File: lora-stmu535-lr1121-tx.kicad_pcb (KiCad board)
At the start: 4 copper layers, 111 parts, among them J1 Conn_Coaxial_Small, J2 Conn_02x07_Odd_Even, J4 USB_C_Receptacle_USB2.0_16P, J5 2.4Ghz Antenna, J6 Conn_01x03_Pin, J7 Conn_02x06_Counter_Clockwise, SW3 SW_Push, U1 BME280, U2 BGS12WN6E6327, U3 BQ25570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

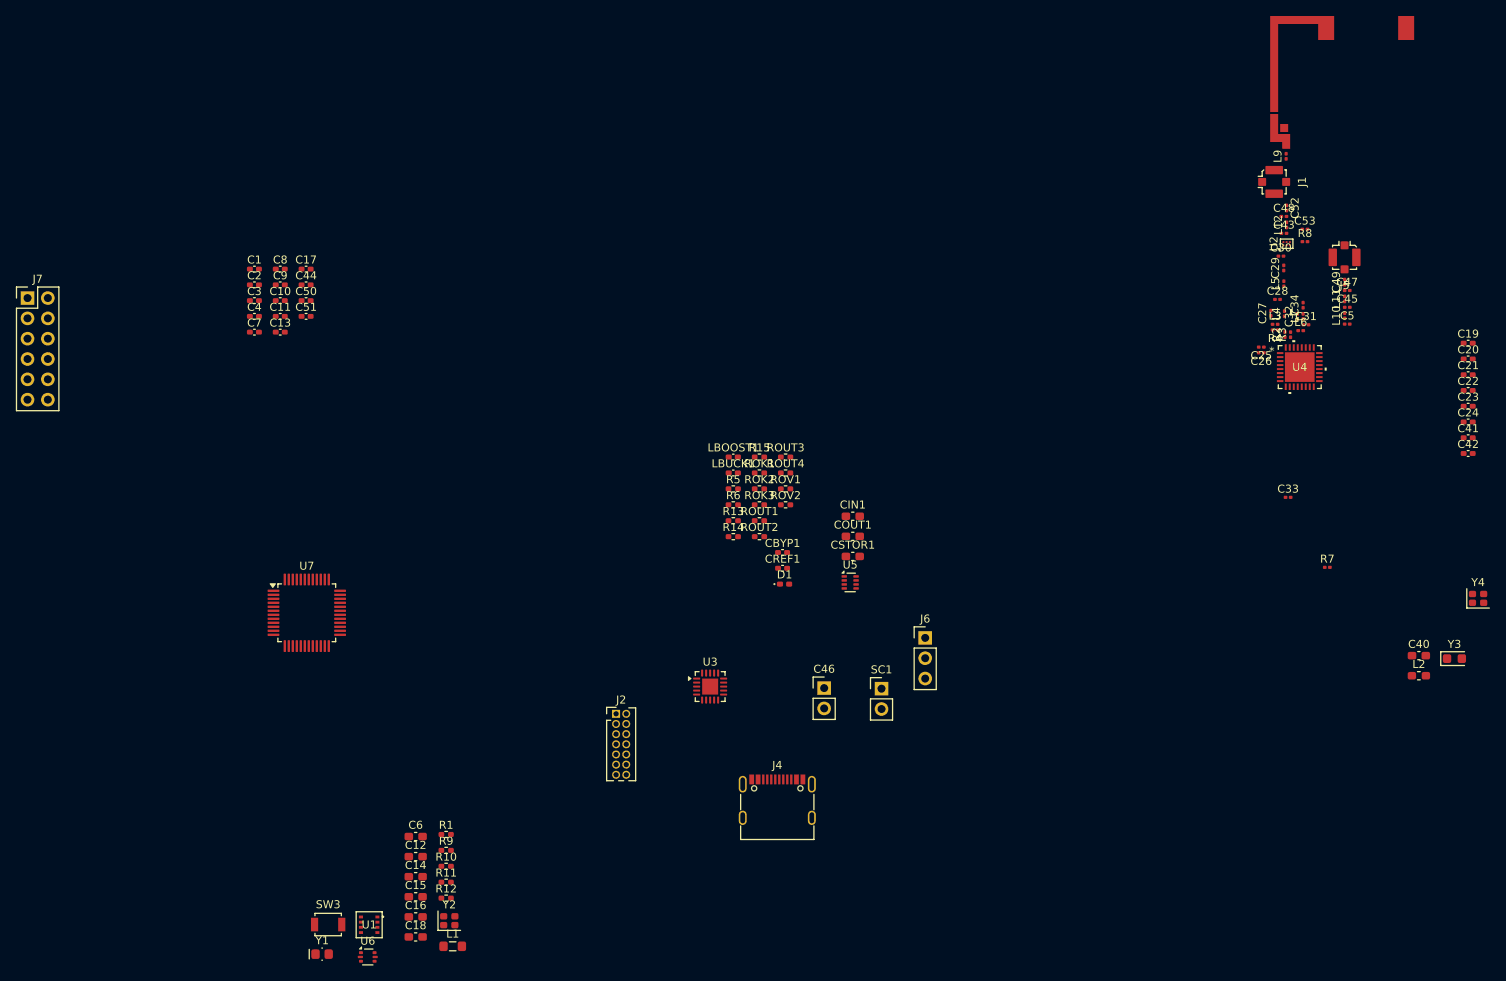
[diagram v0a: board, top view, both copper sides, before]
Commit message: RF and initial routing
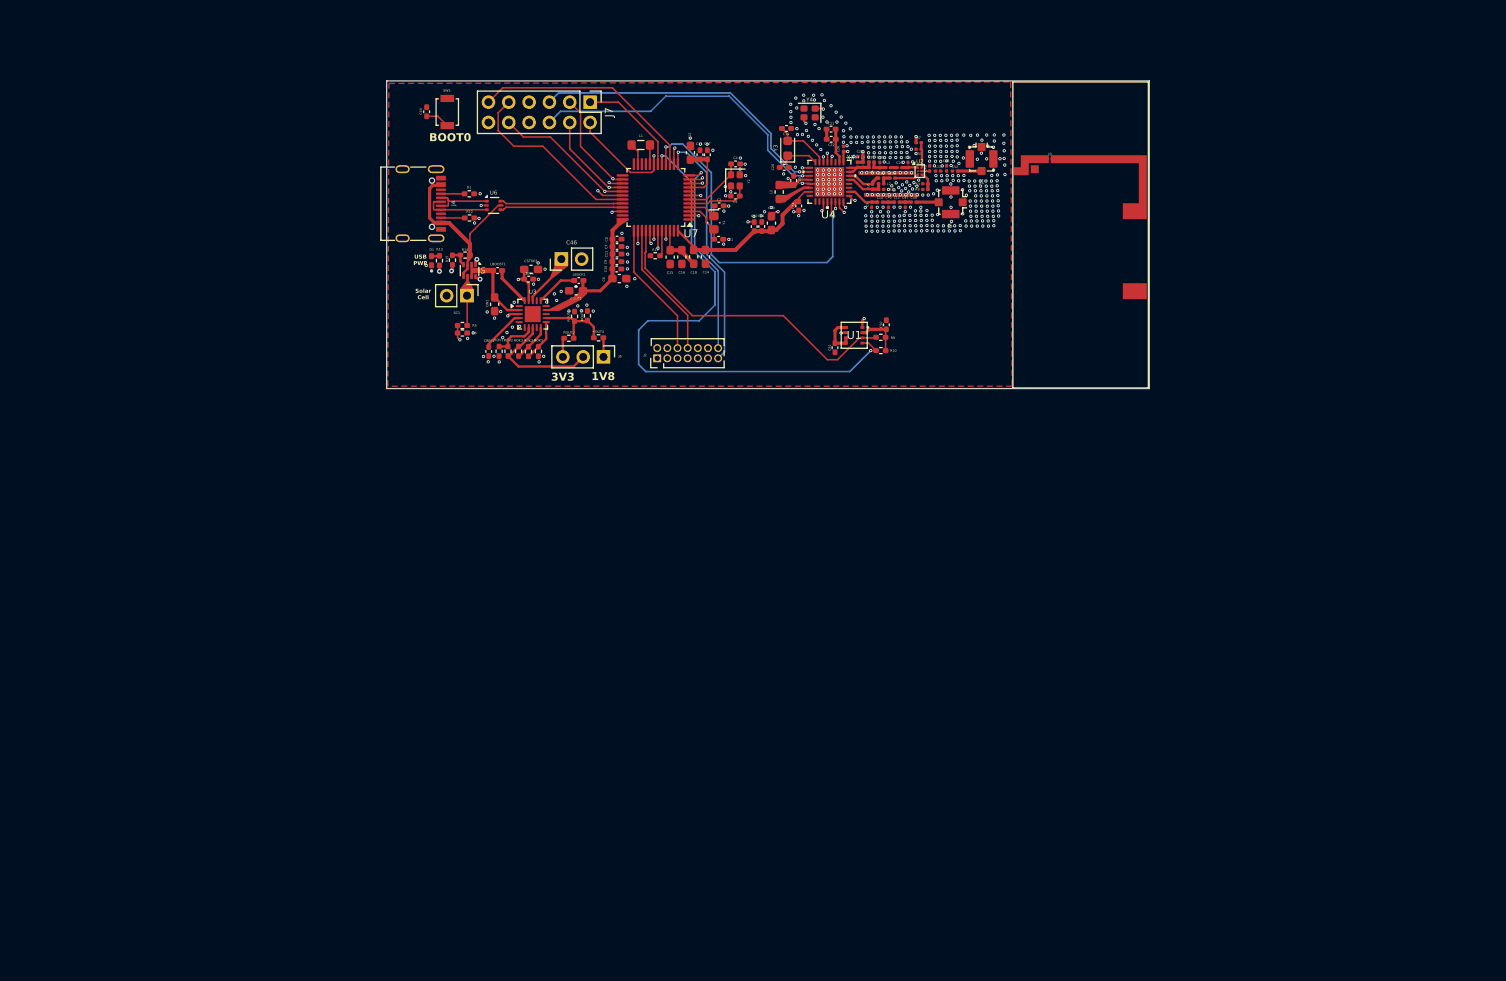
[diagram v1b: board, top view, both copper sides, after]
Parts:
- removed R2, R3: 0R, Resistor_SMD:R_0201_0603Metric
- moved Y3 105.0 mm to (149.4, 59.7), turned to 90 degrees
- moved Y1 103.7 mm to (140.1, 69.0), turned to -90 degrees
- moved Y4 103.3 mm to (152.1, 55.3), turned to 180 degrees
- moved L1 102.9 mm to (131.0, 59.3), turned to 180 degrees
- moved SW3 102.6 mm to (106.8, 55.2), turned to 90 degrees
- moved L2 100.2 mm to (148.3, 65.2), turned to 90 degrees
- moved Y2 99.2 mm to (142.8, 63.7), turned to -90 degrees
- moved C40 97.3 mm to (147.3, 69.1), turned to 90 degrees
- moved U1 95.4 mm to (157.7, 83.1)
- moved U6 95.3 mm to (112.6, 66.9)
- moved C12 94.4 mm to (137.2, 60.3), turned to 90 degrees
- moved C42 93.6 mm to (145.2, 69.5), turned to 90 degrees
- moved C41 92.2 mm to (146.1, 69.5), turned to 90 degrees
- moved C18 91.8 mm to (137.6, 73.3), turned to -90 degrees
- moved C19 89.3 mm to (149.2, 57.2), turned to 180 degrees
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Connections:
- C27 pad 1: Net-(C27-Pad1) -> Net-(U4-RFO_HP_LF)
- J4 pad A6: /MCU/D+ -> Net-(J4-D+-PadA6)
- J4 pad A7: /MCU/D- -> Net-(J4-D--PadA7)
- J4 pad B6: /MCU/D+ -> Net-(J4-D+-PadA6)
- J4 pad B7: /MCU/D- -> Net-(J4-D--PadA7)
- L3 pad 2: Net-(C27-Pad1) -> Net-(U4-RFO_HP_LF)
- L4 pad 1: Net-(C27-Pad1) -> Net-(U4-RFO_HP_LF)
- R4 pad 1: Net-(C27-Pad1) -> Net-(U4-RFO_HP_LF)
- U4 pad 31: Net-(U4-RFO_LP_LF) -> Net-(U4-RFO_HP_LF)
- U6 pad 1: Net-(U7-PA11) -> Net-(J4-D--PadA7)
- U6 pad 3: Net-(U7-PA12) -> Net-(J4-D+-PadA6)
- U6 pad 5: unconnected-(U6-VBUS-Pad5) -> 5V
- U7 pad 32: Net-(U7-PA11) -> /MCU/D-
- U7 pad 33: Net-(U7-PA12) -> /MCU/D+
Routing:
- net SCL: track 0.00 -> 71.0 mm, vias 0 -> 2
- net VBAT: track 0.00 -> 55.1 mm
- net LR_MISO: track 0.00 -> 42.6 mm, vias 0 -> 2
- net SDA: track 0.00 -> 39.5 mm
- net DIO7: track 0.00 -> 39.2 mm, vias 0 -> 1
- net DIO8: track 0.00 -> 38.2 mm, vias 0 -> 1
- net LR_BUSY: track 0.00 -> 36.7 mm, vias 0 -> 2
- net LR_CS: track 0.00 -> 35.1 mm, vias 0 -> 2
- net LR_MOSI: track 0.00 -> 34.5 mm, vias 0 -> 2
- net LR_NRESET: track 0.00 -> 34.0 mm, vias 0 -> 2
- net /MCU/PA0: track 0.00 -> 32.8 mm, vias 0 -> 1
- net /MCU/LPUART_RX: track 0.00 -> 30.6 mm, vias 0 -> 1
- net DIO9: track 0.00 -> 29.0 mm, vias 0 -> 2
- net /MCU/PA5: track 0.00 -> 28.8 mm
- net /MCU/LPUART_TX: track 0.00 -> 25.1 mm, vias 0 -> 1
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- added copper zone on F.Cu, net GND
- added copper zone on In1.Cu, net GND
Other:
- board outline added: 95.3 x 38.4 mm
- board text added: "1V8"
- board text added: "3V3"
- board text added: "BOOT0"
- board text added: "CHECK CLOCK, CHOOSE TCXO/XTAL"
- board text added: "Posso far passare sotto senza problemi?"
- board text added: "Solar Cell"
- board text added: "TODO: - Finish RF - GND - Signal routing - Labeling"
- board text added: "USB PWR"

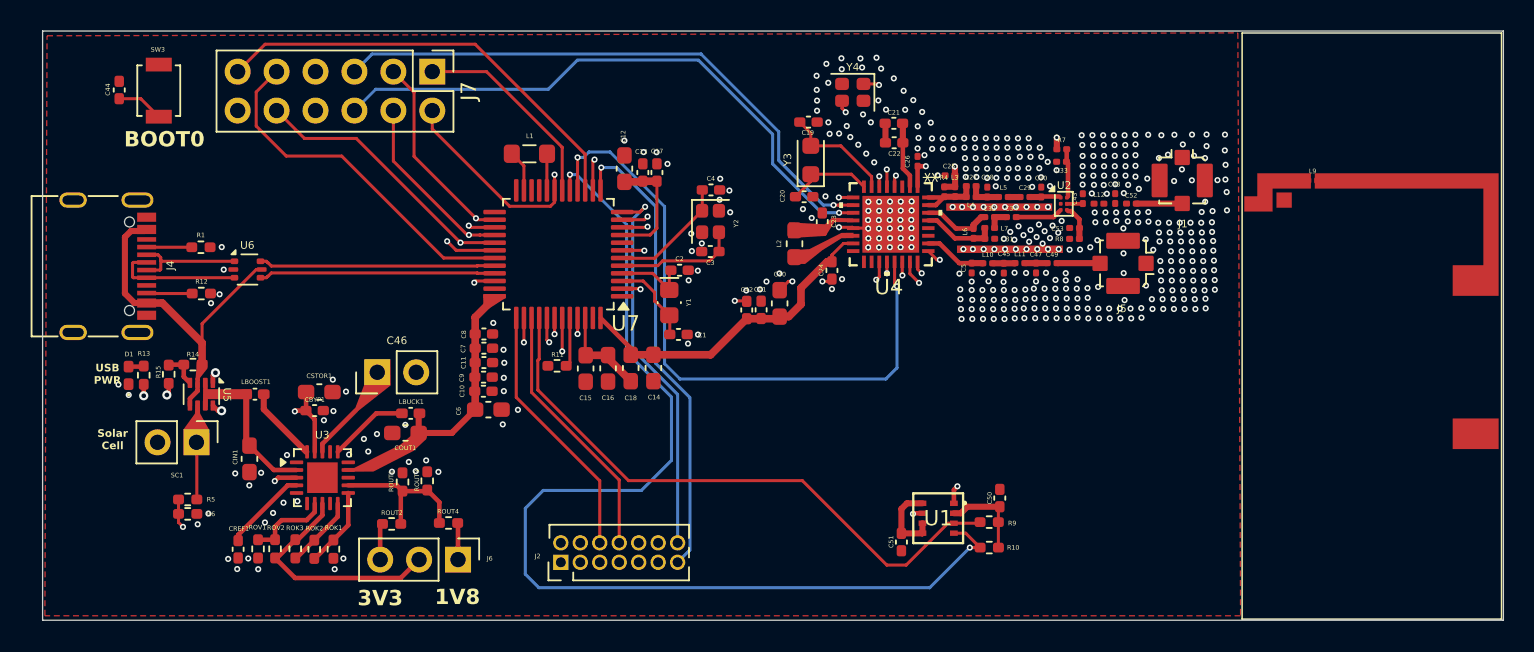
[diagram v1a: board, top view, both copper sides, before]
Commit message: fix DRC errors and antenna
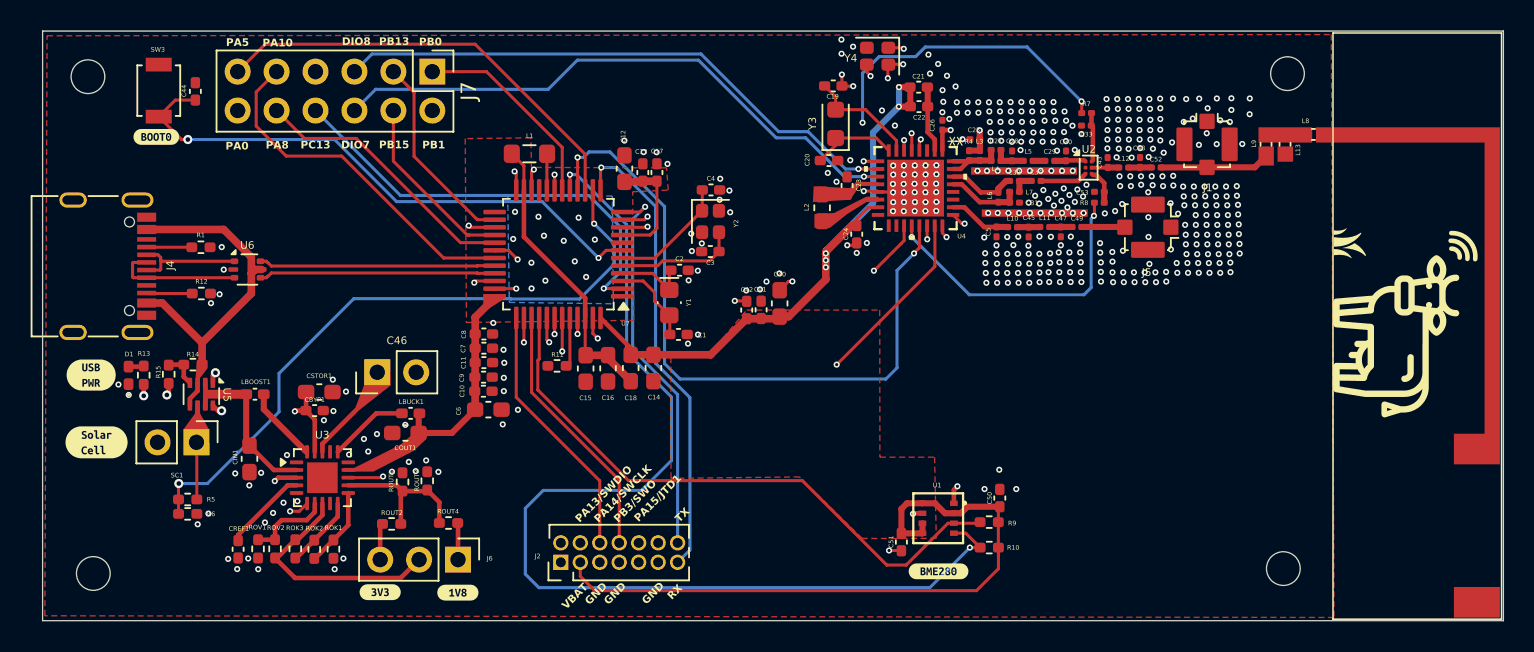
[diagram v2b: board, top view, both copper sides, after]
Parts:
- added L13: 7nH, Inductor_SMD:L_0402_1005Metric_Pad0.77x0.64mm_HandSolder, F.Cu at (180.3, 58.7)
- added L8: 13nH, Inductor_SMD:L_0402_1005Metric_Pad0.77x0.64mm_HandSolder, F.Cu at (182.2, 58.0)
- added REF**: MountingHole_2.2mm_M2, MountingHole:MountingHole_2.2mm_M2, F.Cu at (102.2, 54.3)
- added REF**: MountingHole_2.2mm_M2, MountingHole:MountingHole_2.2mm_M2, F.Cu at (180.5, 54.1)
- added REF**: cow_logo, cowtag:cow_logo, F.Cu at (187.8, 72.3)
- added REF**: MountingHole_2.2mm_M2, MountingHole:MountingHole_2.2mm_M2, F.Cu at (102.6, 86.7)
- added REF**: MountingHole_2.2mm_M2, MountingHole:MountingHole_2.2mm_M2, F.Cu at (180.2, 86.4)
- added REF**: leat, cowtag:leat, B.Cu at (165.7, 85.9)
- added kibuzzard-69E8EEB9: G***, kibuzzard-69E8EEB9, F.Cu at (157.7, 86.5)
- added kibuzzard-69E8EEEB: G***, kibuzzard-69E8EEEB, F.Cu at (121.3, 87.9)
- added kibuzzard-69E8EEF7: G***, kibuzzard-69E8EEF7, F.Cu at (126.3, 87.9)
- added kibuzzard-69E8EF24: G***, kibuzzard-69E8EF24, F.Cu at (102.4, 73.7)
- added kibuzzard-69E8EF49: G***, kibuzzard-69E8EF49, F.Cu at (102.8, 78.1)
- added kibuzzard-69E8EF58: G***, kibuzzard-69E8EF58, F.Cu at (106.7, 58.2)
- L9: value 39nH -> 1.3nH; footprint Inductor_SMD:L_0201_0603Metric -> Inductor_SMD:L_0402_1005Metric_Pad0.77x0.64mm_HandSolder
- moved C44 4.97 mm to (109.2, 55.2)
- moved L9 3.86 mm to (179.1, 58.7), turned to 90 degrees
- moved AE1 3.00 mm to (176.8, 57.1)
- moved L2 2.96 mm to (150.1, 62.8)
- moved C22 2.86 mm to (156.4, 56.2)
- moved R8 2.86 mm to (168.2, 62.5)
- moved Y3 2.86 mm to (151.0, 57.3)
- moved C19 2.86 mm to (150.8, 54.9)
- moved C20 2.86 mm to (150.6, 59.7)
- moved C21 2.86 mm to (156.4, 55.0)
- moved C23 2.86 mm to (151.8, 61.4)
- moved C24 2.86 mm to (152.4, 64.6)
- moved C25 2.86 mm to (160.1, 58.4)
- moved C26 2.86 mm to (158.0, 57.4)
- moved C27 2.86 mm to (161.5, 59.1)
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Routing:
- net VBAT: track 55.1 -> 106.2 mm, vias 0 -> 17
- net ADC_SOLAR: track 3.98 -> 43.2 mm
- net /MCU/NRST: track 4.52 -> 37.2 mm, vias 1 -> 2
- net /RF/RFSW1: track 2.02 -> 34.3 mm, vias 2 -> 3
- net LR_SCK: track 3.37 -> 34.6 mm
- net /MCU/PC13: track 1.21 -> 28.7 mm
- net VBAT_OK: track 3.34 -> 23.1 mm, vias 1 -> 2
- net /RF/RFSW0: track 0.75 -> 19.8 mm, vias 1 -> 2
- net VDD11: track 8.94 -> 18.9 mm
- net GND: track 9.62 -> 19.4 mm, vias 448 -> 426
- net /BQ25570/VOC_SAMP: track 11.7 -> 17.6 mm, vias 2 -> 3
- net /RF/868_RF: track 3.00 -> 7.16 mm
- net LR_NRESET: track 34.0 -> 37.6 mm
- net LR_BUSY: track 36.7 -> 39.7 mm
- net LR_MOSI: track 34.5 -> 37.4 mm
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- added copper zone on B.Cu, net VBAT
- added copper zone on F.Cu, net VBAT
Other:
- board size 95.3 x 38.4 mm -> 95.3 x 38.5 mm
- board text added: "CowTag v0.1"
- board text added: "DIO7"
- board text added: "DIO8"
- board text added: "GND"
- board text added: "PA0"
- board text added: "PA10"
- board text added: "PA13/SWDIO"
- board text added: "PA14/SWCLK"
- board text added: "PA15/JTD1"
- board text added: "PA5"
- board text added: "PA8"
- board text added: "PB0"
- board text added: "PB1"
- board text added: "PB13"
- board text added: "PB15"
- board text added: "PB3/SWO"
- board text added: "PC13"
- board text added: "RX"
- board text added: "TODO: - Recheck RF - Labeling - Vias"
- board text added: "TX"
- board text added: "VBAT"
- board text removed: "1V8"
- board text removed: "3V3"
- board text removed: "BOOT0"
- board text removed: "CHECK CLOCK, CHOOSE TCXO/XTAL"
- board text removed: "Posso far passare sotto senza problemi?"
- board text removed: "Solar Cell"
- board text removed: "TODO: - Finish RF - GND - Signal routing - Labeling"
- board text removed: "USB PWR"

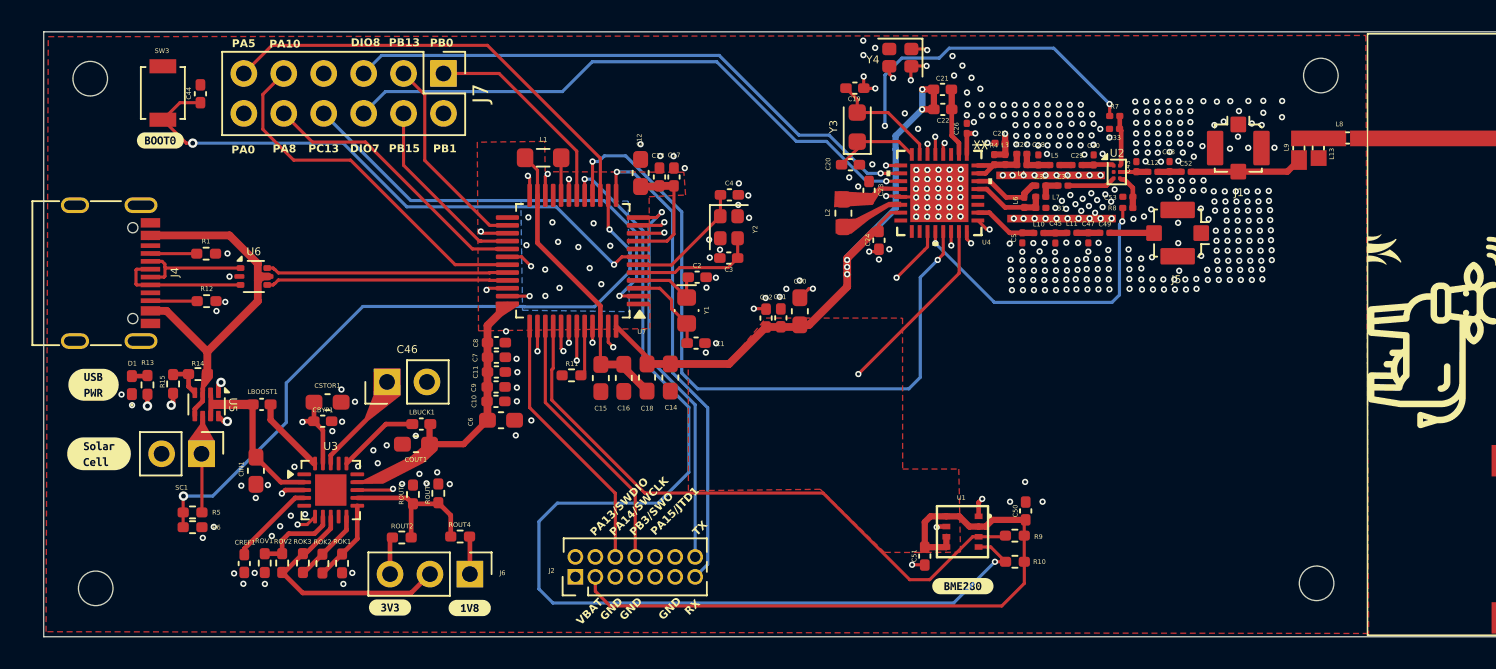
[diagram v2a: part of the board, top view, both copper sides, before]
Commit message: labeling and via placing
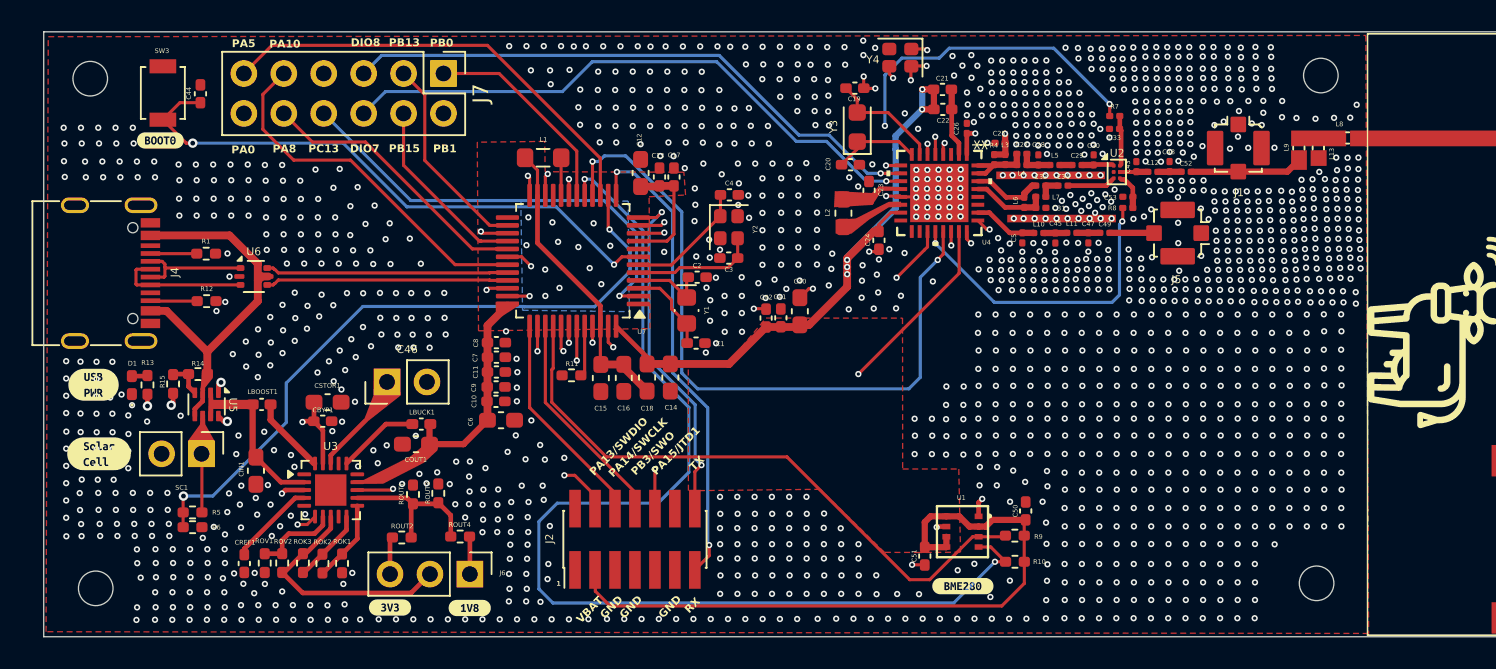
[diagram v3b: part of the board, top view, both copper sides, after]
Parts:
- removed kibuzzard-69E8EEB9: G***, kibuzzard-69E8EEB9
- added kibuzzard-69E8FA9E: G***, kibuzzard-69E8FA9E, F.Cu at (157.7, 86.5)
- J2: footprint Connector_PinHeader_1.27mm:PinHeader_2x07_P1.27mm_Vertical -> Connector_PinHeader_1.27mm:PinHeader_2x07_P1.27mm_Vertical_SMD
- moved J2 4.48 mm to (136.9, 83.6)
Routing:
- net /MCU/PA14/SWCLK: track 16.9 -> 13.9 mm
- net /MCU/PB3/TRACESWO: track 17.0 -> 14.0 mm
- net /MCU/PA15/JTDI: track 17.8 -> 14.7 mm, vias 1 -> 2
- net /MCU/LPUART_TX: track 25.1 -> 22.4 mm, vias 1 -> 2
- net /MCU/PA13/SWDIO: track 22.3 -> 21.5 mm, vias 1 -> 2
- net /MCU/LPUART_RX: track 30.6 -> 30.2 mm, vias 1 -> 2
- net GND: vias 426 -> 1606
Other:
- board text added: "1"
- board text added: "TODO: - Recheck RF"
- board text removed: "TODO: - Recheck RF - Labeling - Vias"
